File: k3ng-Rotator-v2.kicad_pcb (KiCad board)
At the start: 6 copper layers, 93 x 54.5 mm, 21 parts, among them J1 1844922, J2 1844922, U1 DRV8871DDA, U2 DRV8871DDA

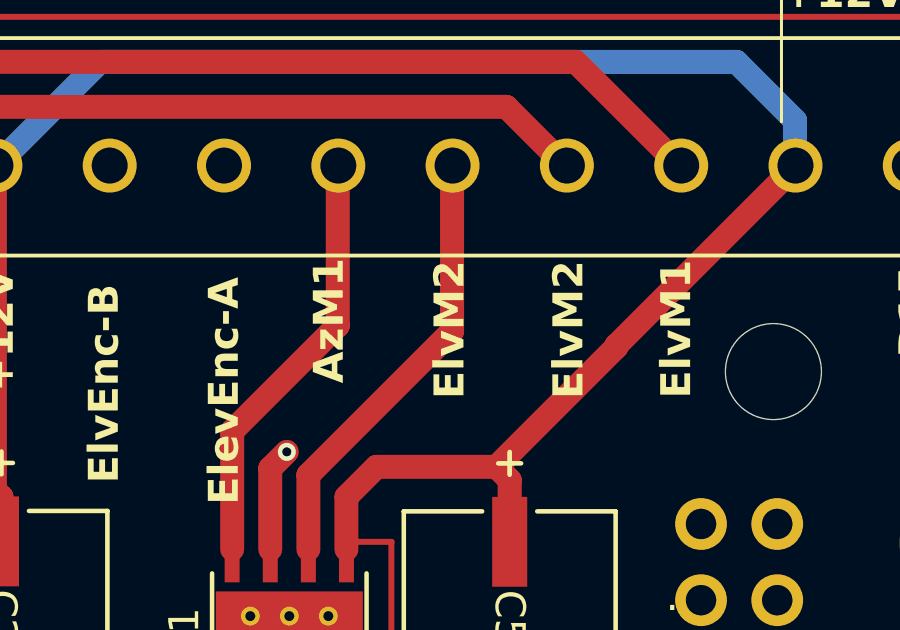
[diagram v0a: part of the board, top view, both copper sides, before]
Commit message: Fix silkscreen, add drawing and step file and dxf for stencil
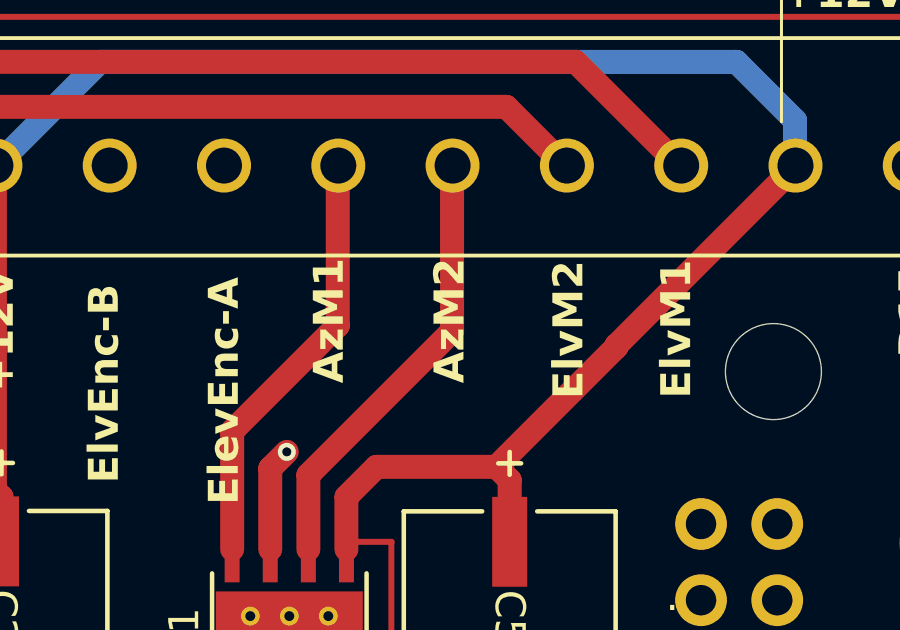
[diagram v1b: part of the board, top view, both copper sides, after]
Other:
- board text added: "AzM2"
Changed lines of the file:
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@@
 		(tenting front back)
 		(pcbplotparams
-			(layerselection 0x00000000_00000000_55555555_5755f5ff)
-			(plot_on_all_layers_selection 0x00000000_00000000_00000000_00000000)
+			(layerselection 0x00000000_00000000_55555555_55557000)
+			(plot_on_all_layers_selection 0x00000000_00000000_00000000_00000002)
 			(disableapertmacros no)
 			(usegerberextensions no)
@@
 			(pdf_single_document no)
 			(dxfpolygonmode yes)
-			(dxfimperialunits yes)
+			(dxfimperialunits no)
 			(dxfusepcbnewfont yes)
 			(psnegative no)
@@
 			(crossoutdnponfab yes)
 			(subtractmaskfromsilk no)
-			(outputformat 1)
+			(outputformat 3)
 			(mirror no)
 			(drillshape 0)
@@
 		)
 	)
-	(gr_text "ElvM2"
-		(at 139.020858 75.738096 90)
+	(gr_text "AzM2"
+		(at 139.020858 75.214286 90)
 		(layer "F.SilkS" knockout)
 		(effects
